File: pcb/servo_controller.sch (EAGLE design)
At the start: 52 parts, among them IC1 PIC18F452, IC2 LM2936MP-3.0, Q1 10Mhz, U1 ARDUINOR3-DIMENSION

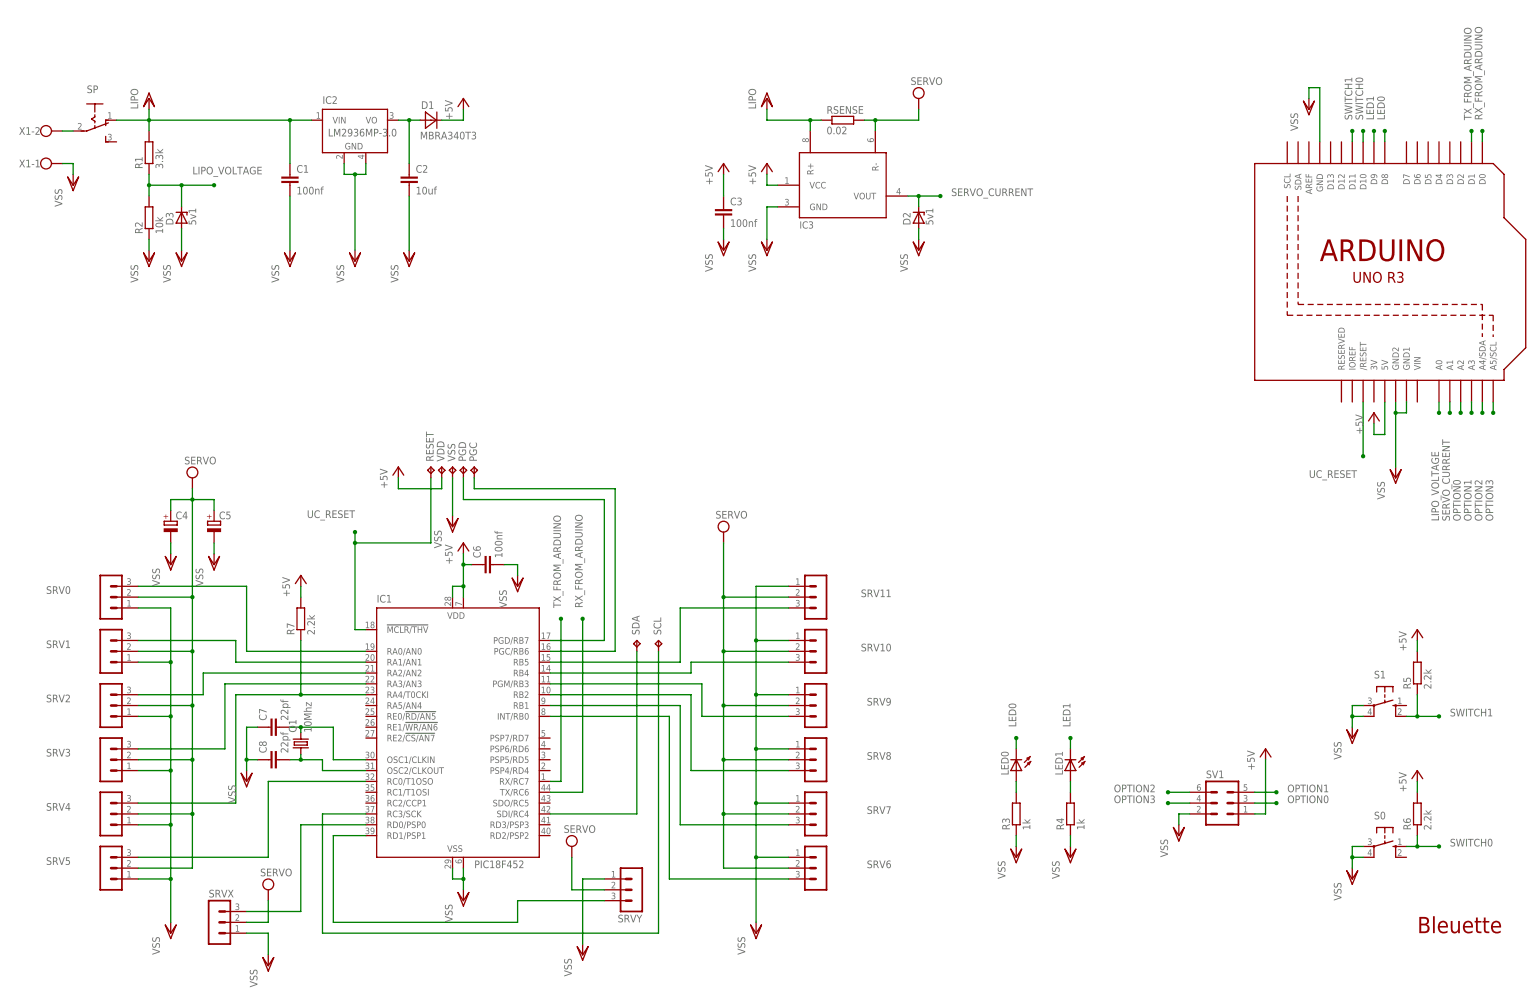
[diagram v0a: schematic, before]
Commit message: Rev 1.2.0
- Added C9 for better 5V filter
- Added reset jumper
- Added OpenHardware logo
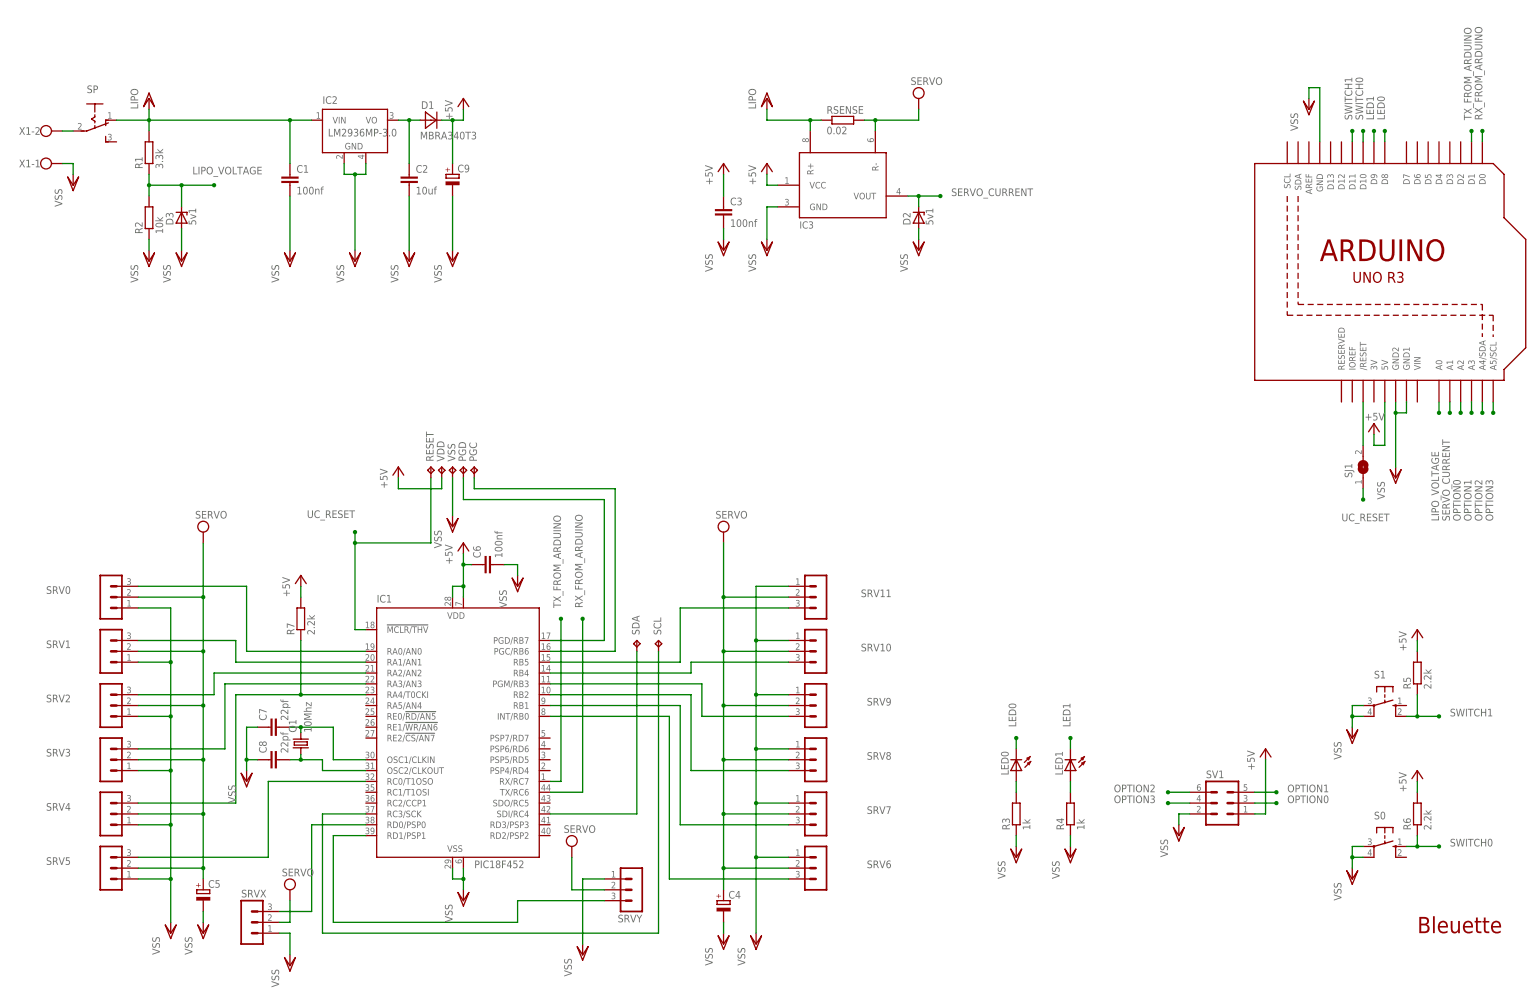
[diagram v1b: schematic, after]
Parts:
- added C9: (no value), rcl:CPOL-EUF
- added SJ1: (no value), jumper:SJ
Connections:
- new net N$16: SJ1.2, U1./RESET
- net +5V: now also C9.+
- net UC_RESET: now also SJ1.1; no longer U1./RESET
- net VSS: now also C9.-
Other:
- moved on the sheet: C4, C5, SRVX

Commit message: Rev. 1.2.1
- Change switch to 2.54mm one
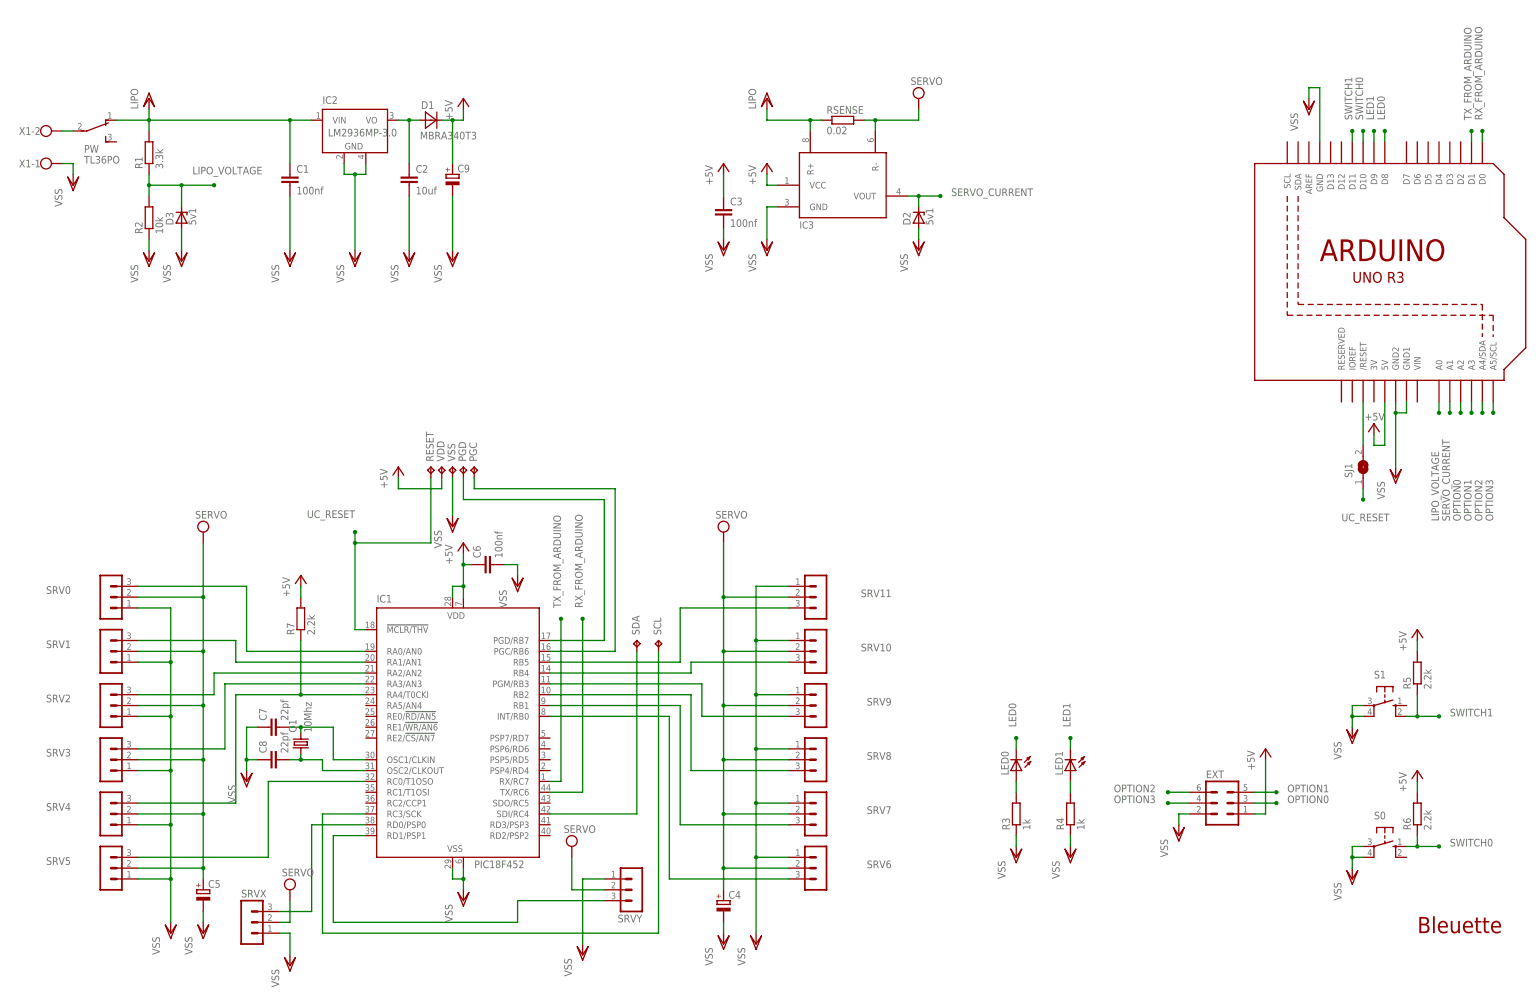
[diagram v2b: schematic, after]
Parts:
- removed SP: (no value), switch:255SB
- added PW: TL36PO, switch:TL36PO
- renumbered SV1 to EXT
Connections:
- net N$15: now also PW.P; no longer SP.P
- net VDD: now also PW.O; no longer SP.O
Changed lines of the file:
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@@
 <setting verticaltext="up"/>
 </settings>
-<grid distance="0.1" unitdist="inch" unit="inch" style="dots" multiple="1" display="yes" altdistance="0.01" altunitdist="inch" altunit="inch"/>
+<grid distance="0.1" unitdist="inch" unit="inch" style="lines" multiple="1" display="no" altdistance="0.01" altunitdist="inch" altunit="inch"/>
 <layers>
 <layer number="1" name="Top" color="4" fill="1" visible="no" active="no"/>
@@
 <part name="R2" library="rcl" deviceset="R-EU_" device="M1206" value="10k"/>
 <part name="VSS6" library="supply1" deviceset="VSS" device=""/>
-<part name="SP" library="switch" deviceset="255SB" device=""/>
 <part name="P+1" library="supply1" deviceset="+5V" device=""/>
 <part name="P+8" library="supply1" deviceset="+5V" device=""/>
@@
 <part name="P+6" library="supply1" deviceset="+5V" device=""/>
 <part name="VSS8" library="supply1" deviceset="VSS" device=""/>
-<part name="SV1" library="con-lstb" deviceset="MA03-2" device=""/>
+<part name="EXT" library="con-lstb" deviceset="MA03-2" device=""/>
 <part name="C5" library="rcl" deviceset="CPOL-EU" device="D"/>
 <part name="VSS22" library="supply1" deviceset="VSS" device=""/>
@@
 <part name="C9" library="rcl" deviceset="CPOL-EU" device="F"/>
 <part name="VSS27" library="supply1" deviceset="VSS" device=""/>
+<part name="PW" library="switch" deviceset="TL36PO" device=""/>
 </parts>
 <sheets>
@@
 <instance part="R2" gate="G$1" x="48.26" y="187.96" rot="R90"/>
 <instance part="VSS6" gate="G$1" x="48.26" y="177.8"/>
-<instance part="SP" gate="1" x="35.56" y="210.82" rot="R270"/>
 <instance part="P+1" gate="1" x="121.92" y="215.9"/>
 <instance part="P+8" gate="1" x="193.04" y="200.66"/>
@@
 <instance part="P+6" gate="1" x="182.88" y="200.66"/>
 <instance part="VSS8" gate="G$1" x="182.88" y="180.34"/>
-<instance part="SV1" gate="1" x="299.72" y="50.8"/>
+<instance part="EXT" gate="1" x="299.72" y="50.8"/>
 <instance part="C5" gate="G$1" x="60.96" y="30.48"/>
 <instance part="VSS22" gate="G$1" x="60.96" y="20.32"/>
@@
 <instance part="C9" gate="G$1" x="119.38" y="198.12"/>
 <instance part="VSS27" gate="G$1" x="119.38" y="177.8"/>
+<instance part="PW" gate="BEF1" x="35.56" y="208.28" rot="R270"/>
 </instances>
 <busses>
@@
 <pinref part="VSS13" gate="G$1" pin="VSS"/>
 <wire x1="289.56" y1="48.26" x2="289.56" y2="45.72" width="0.1524" layer="91"/>
-<pinref part="SV1" gate="1" pin="2"/>
+<pinref part="EXT" gate="1" pin="2"/>
 </segment>
 <segment>
@@
 <pinref part="P+11" gate="1" pin="+5V"/>
 <wire x1="309.88" y1="48.26" x2="309.88" y2="60.96" width="0.1524" layer="91"/>
-<pinref part="SV1" gate="1" pin="1"/>
+<pinref part="EXT" gate="1" pin="1"/>
 </segment>
 <segment>
@@
 <pinref part="R1" gate="G$1" pin="2"/>
 <wire x1="48.26" y1="210.82" x2="48.26" y2="208.28" width="0.1524" layer="91"/>
-<pinref part="SP" gate="1" pin="O"/>
 <wire x1="40.64" y1="210.82" x2="48.26" y2="210.82" width="0.1524" layer="91"/>
 <junction x="48.26" y="210.82"/>
@@
 <wire x1="48.26" y1="210.82" x2="48.26" y2="213.36" width="0.1524" layer="91"/>
 <pinref part="IC2" gate="G$1" pin="VIN"/>
+<pinref part="PW" gate="BEF1" pin="O"/>
 </segment>
 <segment>
@@
 <net name="OPTION0" class="0">
 <segment>
-<pinref part="SV1" gate="1" pin="3"/>
+<pinref part="EXT" gate="1" pin="3"/>
 <wire x1="307.34" y1="50.8" x2="312.42" y2="50.8" width="0.1524" layer="91"/>
 <junction x="312.42" y="50.8"/>
@@
 </segment>
 <segment>
-<pinref part="SV1" gate="1" pin="6"/>
+<pinref part="EXT" gate="1" pin="6"/>
 <wire x1="292.1" y1="53.34" x2="287.02" y2="53.34" width="0.1524" layer="91"/>
 <junction x="287.02" y="53.34"/>
@@
 </segment>
 <segment>
-<pinref part="SV1" gate="1" pin="4"/>
+<pinref part="EXT" gate="1" pin="4"/>
 <wire x1="292.1" y1="50.8" x2="287.02" y2="50.8" width="0.1524" layer="91"/>
 <junction x="287.02" y="50.8"/>
@@
 </segment>
 <segment>
-<pinref part="SV1" gate="1" pin="5"/>
+<pinref part="EXT" gate="1" pin="5"/>
 <wire x1="307.34" y1="53.34" x2="312.42" y2="53.34" width="0.1524" layer="91"/>
 <junction x="312.42" y="53.34"/>
@@
 <net name="N$15" class="0">
 <segment>
-<pinref part="SP" gate="1" pin="P"/>
 <pinref part="X1" gate="-2" pin="KL"/>
 <wire x1="27.94" y1="208.28" x2="30.48" y2="208.28" width="0.1524" layer="91"/>
-</segment>
-</net>
+<pinref part="PW" gate="BEF1" pin="P"/>
+</segment>
+</net>
